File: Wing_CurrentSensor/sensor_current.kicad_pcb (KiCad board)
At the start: 2 copper layers, 50.8 x 22.9 mm, 25 parts, among them J1 feather long, J2 feather short, J3 SJ-3524-SMT, J4 Analog Selection, U1 TL084, U2 AD8226

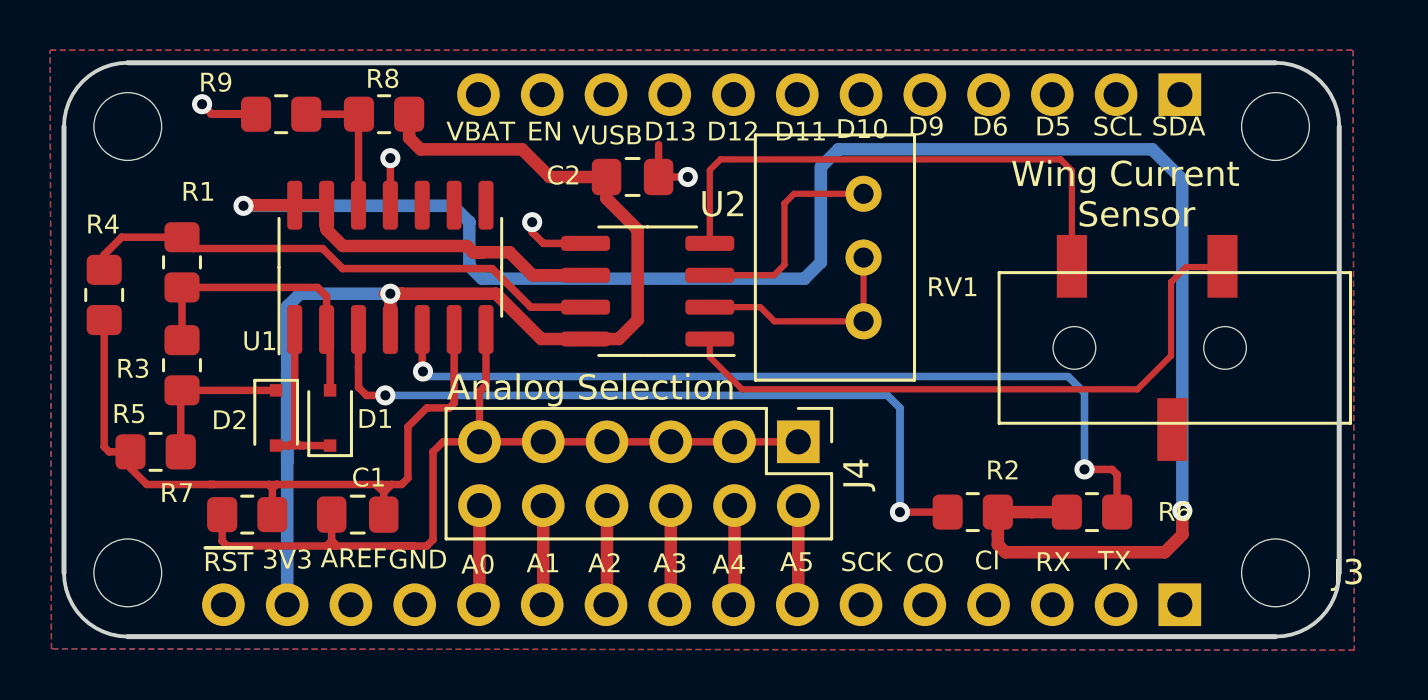
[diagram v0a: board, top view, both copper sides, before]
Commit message: Change_name_add connector
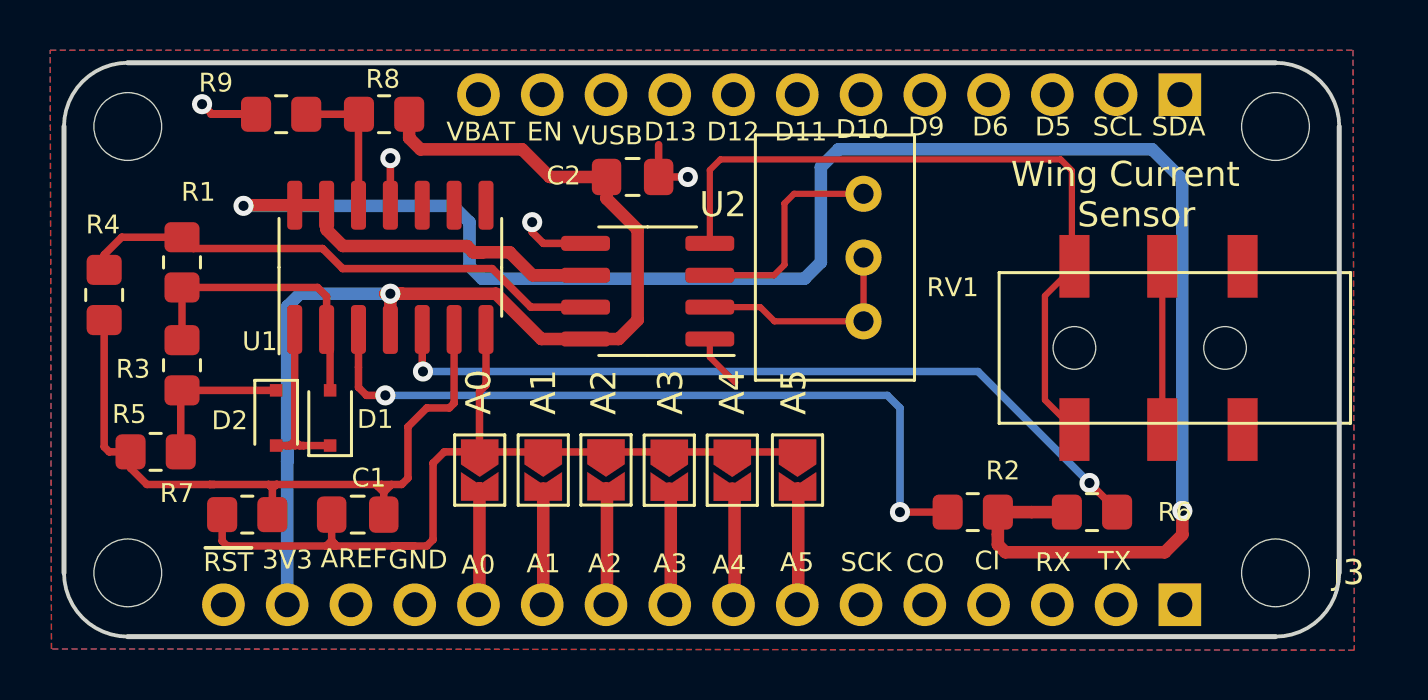
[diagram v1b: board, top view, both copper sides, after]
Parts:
- removed J4: Analog Selection, Connector_PinHeader_2.54mm:PinHeader_2x06_P2.54mm_Vertical
- added A0: A0, Jumper:SolderJumper-2_P1.3mm_Open_TrianglePad1.0x1.5mm, F.Cu at (124.6, 106.6)
- added A1: A1, Jumper:SolderJumper-2_P1.3mm_Open_TrianglePad1.0x1.5mm, F.Cu at (127.1, 106.6)
- added A2: A2, Jumper:SolderJumper-2_P1.3mm_Open_TrianglePad1.0x1.5mm, F.Cu at (129.6, 106.6)
- added A3: A3, Jumper:SolderJumper-2_P1.3mm_Open_TrianglePad1.0x1.5mm, F.Cu at (132.1, 106.6)
- added A4: A4, Jumper:SolderJumper-2_P1.3mm_Open_TrianglePad1.0x1.5mm, F.Cu at (134.6, 106.6)
- added A5: A5, Jumper:SolderJumper-2_P1.3mm_Open_TrianglePad1.0x1.5mm, F.Cu at (137.2, 106.6)
- J3: value SJ-3524-SMT -> PJ-320B
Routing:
- net GND: track 36.6 -> 13.3 mm
- net /IN+: track 21.5 -> 29.0 mm
- net Net-(J3-Pad2): track 0.00 -> 6.50 mm
- net Net-(R6-Pad1): track 34.3 -> 31.7 mm
- net /A4: track 7.36 -> 8.08 mm
- net /A2: track 7.36 -> 8.07 mm
- net /A3: track 7.36 -> 8.07 mm
- net /A5: track 7.36 -> 8.06 mm
- net /A0: track 7.36 -> 8.05 mm
- net /A1: track 7.36 -> 8.05 mm

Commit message: Add_3D_Models_Add_Diode
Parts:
- moved A0 0.61 mm to (124.6, 107.2)
- moved A1 0.61 mm to (127.1, 107.2)
- moved A2 0.61 mm to (129.6, 107.2)
- moved A4 0.61 mm to (134.7, 107.2)
- moved A5 0.61 mm to (137.2, 107.2)
- moved A3 0.61 mm to (132.1, 107.2)
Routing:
- net /A4: track 8.08 -> 4.03 mm
- net /A3: track 8.07 -> 4.03 mm
- net /A2: track 8.07 -> 4.05 mm
- net /A5: track 8.06 -> 4.05 mm
- net /A0: track 8.05 -> 4.06 mm
- net /A1: track 8.05 -> 4.06 mm
- net /IN+: track 29.0 -> 30.9 mm
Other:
- board text added: "Wing Current Sensor V1.1"
- board text removed: "Wing Current Sensor V1.0"

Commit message: Move_Labels
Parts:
- moved RV1 0.50 mm to (139.8, 101.2)
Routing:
- net GND: track 13.3 -> 16.8 mm, vias 4 -> 6
- net Net-(C1-Pad2): track 29.3 -> 27.9 mm
- net Net-(RV1-Pad3): track 8.93 -> 7.74 mm

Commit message: update v1.0
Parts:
- moved R5 3.61 mm to (110.6, 102.5), turned to 90 degrees
- moved R4 1.62 mm to (110.6, 98.3)
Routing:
- net GND: track 16.8 -> 37.9 mm, vias 6 -> 9
- net Net-(C1-Pad2): track 27.9 -> 31.9 mm
- net /OUT1: track 21.2 -> 19.4 mm
- net Net-(R6-Pad1): track 31.7 -> 33.5 mm
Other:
- board text added: "v1.0"
